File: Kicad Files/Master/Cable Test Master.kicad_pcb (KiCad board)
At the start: 2 copper layers, 50.8 x 61.6 mm, 64 parts, among them J1 RJ45, J2 RJ12, J3 PWR, J4 ISP, Q1 BSS84, Q10 2N7002, Q11 2N7002, Q12 2N7002, Q13 2N7002, Q14 2N7002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

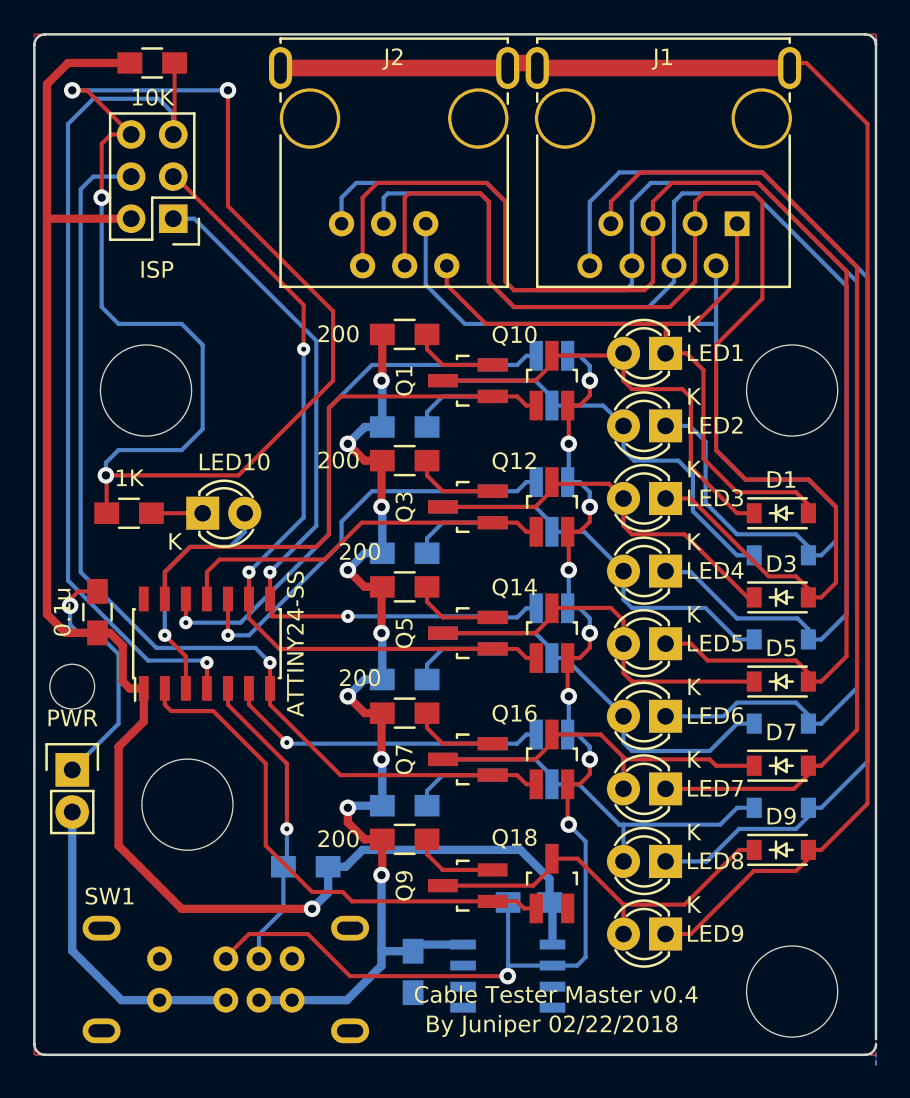
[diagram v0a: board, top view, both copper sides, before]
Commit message: Fix small measurement error in RJ-45 Footprint
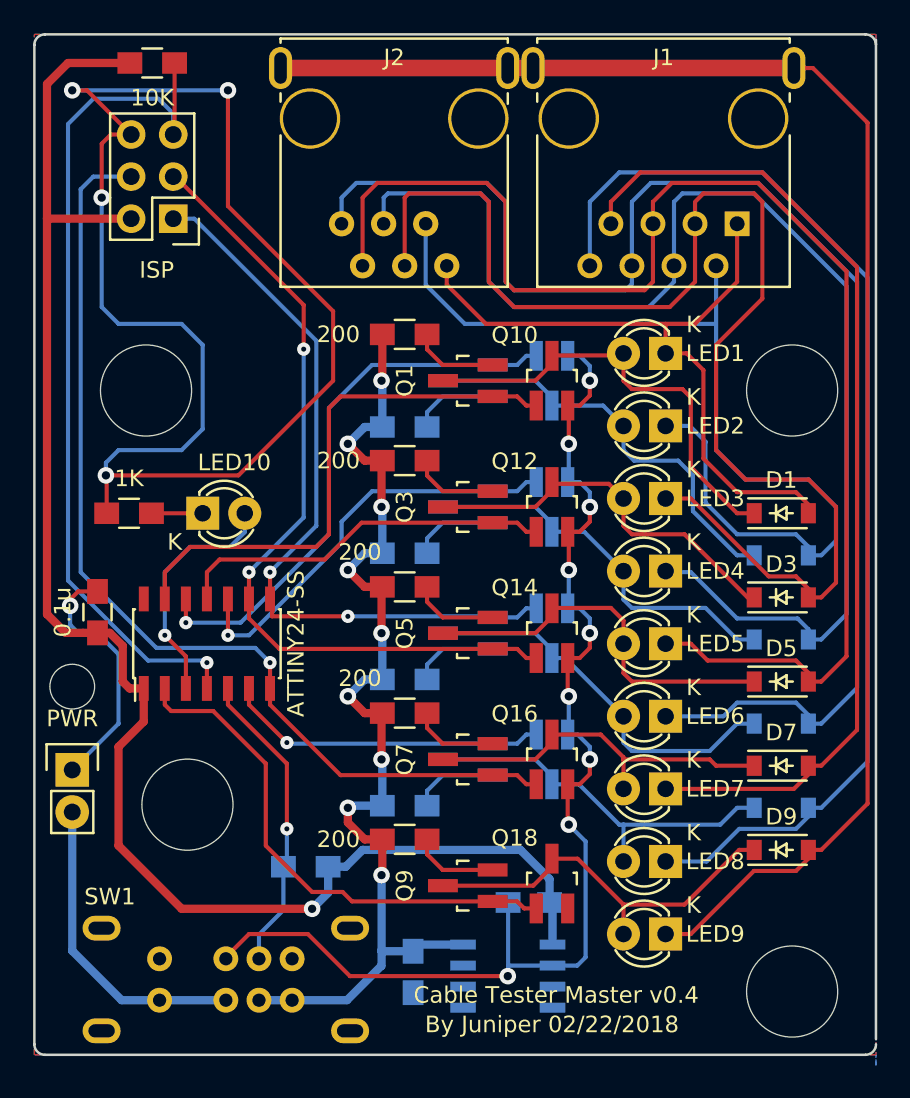
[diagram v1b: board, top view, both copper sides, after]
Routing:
- net /S: track 93.7 -> 93.2 mm
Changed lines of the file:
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@@
     (pad 1 thru_hole circle (at 0 0) (size 5.5 5.5) (drill 5.5) (layers))
-  )
-  (module Tester_Connectors:RJ45_SHLD (layer F.Cu)
-    (at 149.733 68.58 180)
-    (tags RJ45)
-    (fp_text reference J1 (at 0 3.683 180) (layer F.SilkS)
-      (effects (font (size 1 1) (thickness 0.15)))
-    )
-    (fp_text value RJ45 (at 0.14224 -0.1016 180) (layer F.Fab)
-      (effects (font (size 1 1) (thickness 0.15)))
-    )
-    (fp_line (start 7.62 -1.016) (end 7.62 -10.16) (layer F.SilkS) (width 0.15))
-    (fp_line (start 7.62 -10.16) (end -7.62 -10.16) (layer F.SilkS) (width 0.15))
-    (fp_line (start -7.62 -10.16) (end -7.62 -1.016) (layer F.SilkS) (width 0.15))
-    (fp_line (start 7.62 4.572) (end 7.62 4.826) (layer F.SilkS) (width 0.15))
-    (fp_line (start 7.62 4.826) (end -7.62 4.826) (layer F.SilkS) (width 0.15))
-    (fp_line (start -7.62 4.826) (end -7.62 4.572) (layer F.SilkS) (width 0.15))
-    (fp_line (start -7.62 1.524) (end -7.62 1.016) (layer F.SilkS) (width 0.15))
-    (fp_line (start 7.62 1.016) (end 7.62 1.524) (layer F.SilkS) (width 0.15))
-    (pad 9 thru_hole oval (at -7.62 3.048 180) (size 1.397 2.54) (drill oval 0.762 1.905) (layers *.Cu *.Mask F.SilkS)
-      (net 12 /S))
-    (pad "" np_thru_hole circle (at 5.93852 0 180) (size 3.64998 3.64998) (drill 3.2512) (layers *.Cu *.SilkS *.Mask))
-    (pad Hole np_thru_hole circle (at -5.9309 0 180) (size 3.64998 3.64998) (drill 3.2512) (layers *.Cu *.SilkS *.Mask))
-    (pad 1 thru_hole rect (at -4.445 -6.35 180) (size 1.50114 1.50114) (drill 0.89916) (layers *.Cu *.Mask F.SilkS)
-      (net 4 /1))
-    (pad 2 thru_hole circle (at -3.175 -8.89 180) (size 1.50114 1.50114) (drill 0.89916) (layers *.Cu *.Mask F.SilkS)
-      (net 5 /2))
-    (pad 3 thru_hole circle (at -1.905 -6.35 180) (size 1.50114 1.50114) (drill 0.89916) (layers *.Cu *.Mask F.SilkS)
-      (net 6 /3))
-    (pad 4 thru_hole circle (at -0.635 -8.89 180) (size 1.50114 1.50114) (drill 0.89916) (layers *.Cu *.Mask F.SilkS)
-      (net 7 /4))
-    (pad 5 thru_hole circle (at 0.635 -6.35 180) (size 1.50114 1.50114) (drill 0.89916) (layers *.Cu *.Mask F.SilkS)
-      (net 8 /5))
-    (pad 6 thru_hole circle (at 1.905 -8.89 180) (size 1.50114 1.50114) (drill 0.89916) (layers *.Cu *.Mask F.SilkS)
-      (net 9 /6))
-    (pad 7 thru_hole circle (at 3.175 -6.35 180) (size 1.50114 1.50114) (drill 0.89916) (layers *.Cu *.Mask F.SilkS)
-      (net 10 /7))
-    (pad 8 thru_hole circle (at 4.445 -8.89 180) (size 1.50114 1.50114) (drill 0.89916) (layers *.Cu *.Mask F.SilkS)
-      (net 11 /8))
-    (pad 9 thru_hole oval (at 7.62 3.048 180) (size 1.397 2.54) (drill oval 0.762 1.905) (layers *.Cu *.Mask F.SilkS)
-      (net 12 /S))
-    (model Connect.3dshapes/RJ45_8.wrl
-      (at (xyz 0 0 0))
-      (scale (xyz 0.4 0.4 0.4))
-      (rotate (xyz 0 0 0))
-    )
   )
   (module Mounting_Holes:MountingHole_2-7mm locked (layer F.Cu)
@@
     (pad "" np_thru_hole circle (at 5.08 0 180) (size 3.64998 3.64998) (drill 3.2512) (layers *.Cu *.Mask F.SilkS))
     (pad "" np_thru_hole circle (at -5.08 0 180) (size 3.64998 3.64998) (drill 3.2512) (layers *.Cu *.Mask F.SilkS))
+  )
+  (module Tester_Connectors:RJ45_SHLD (layer F.Cu)
+    (at 149.733 68.58 180)
+    (tags RJ45)
+    (fp_text reference J1 (at 0 3.683 180) (layer F.SilkS)
+      (effects (font (size 1 1) (thickness 0.15)))
+    )
+    (fp_text value RJ45 (at 0.14224 -0.1016 180) (layer F.Fab)
+      (effects (font (size 1 1) (thickness 0.15)))
+    )
+    (fp_line (start 7.62 -1.016) (end 7.62 -10.16) (layer F.SilkS) (width 0.15))
+    (fp_line (start 7.62 -10.16) (end -7.62 -10.16) (layer F.SilkS) (width 0.15))
+    (fp_line (start -7.62 -10.16) (end -7.62 -1.016) (layer F.SilkS) (width 0.15))
+    (fp_line (start 7.62 4.572) (end 7.62 4.826) (layer F.SilkS) (width 0.15))
+    (fp_line (start 7.62 4.826) (end -7.62 4.826) (layer F.SilkS) (width 0.15))
+    (fp_line (start -7.62 4.826) (end -7.62 4.572) (layer F.SilkS) (width 0.15))
+    (fp_line (start -7.62 1.524) (end -7.62 1.016) (layer F.SilkS) (width 0.15))
+    (fp_line (start 7.62 1.016) (end 7.62 1.524) (layer F.SilkS) (width 0.15))
+    (pad 9 thru_hole oval (at -7.874 3.048 180) (size 1.397 2.54) (drill oval 0.762 1.905) (layers *.Cu *.Mask F.SilkS)
+      (net 12 /S))
+    (pad "" np_thru_hole circle (at 5.715 0 180) (size 3.64998 3.64998) (drill 3.2512) (layers *.Cu *.SilkS *.Mask))
+    (pad "" np_thru_hole circle (at -5.715 0 180) (size 3.64998 3.64998) (drill 3.2512) (layers *.Cu *.SilkS *.Mask))
+    (pad 1 thru_hole rect (at -4.445 -6.35 180) (size 1.50114 1.50114) (drill 0.89916) (layers *.Cu *.Mask F.SilkS)
+      (net 4 /1))
+    (pad 2 thru_hole circle (at -3.175 -8.89 180) (size 1.50114 1.50114) (drill 0.89916) (layers *.Cu *.Mask F.SilkS)
+      (net 5 /2))
+    (pad 3 thru_hole circle (at -1.905 -6.35 180) (size 1.50114 1.50114) (drill 0.89916) (layers *.Cu *.Mask F.SilkS)
+      (net 6 /3))
+    (pad 4 thru_hole circle (at -0.635 -8.89 180) (size 1.50114 1.50114) (drill 0.89916) (layers *.Cu *.Mask F.SilkS)
+      (net 7 /4))
+    (pad 5 thru_hole circle (at 0.635 -6.35 180) (size 1.50114 1.50114) (drill 0.89916) (layers *.Cu *.Mask F.SilkS)
+      (net 8 /5))
+    (pad 6 thru_hole circle (at 1.905 -8.89 180) (size 1.50114 1.50114) (drill 0.89916) (layers *.Cu *.Mask F.SilkS)
+      (net 9 /6))
+    (pad 7 thru_hole circle (at 3.175 -6.35 180) (size 1.50114 1.50114) (drill 0.89916) (layers *.Cu *.Mask F.SilkS)
+      (net 10 /7))
+    (pad 8 thru_hole circle (at 4.445 -8.89 180) (size 1.50114 1.50114) (drill 0.89916) (layers *.Cu *.Mask F.SilkS)
+      (net 11 /8))
+    (pad 9 thru_hole oval (at 7.874 3.048 180) (size 1.397 2.54) (drill oval 0.762 1.905) (layers *.Cu *.Mask F.SilkS)
+      (net 12 /S))
+    (model Connect.3dshapes/RJ45_8.wrl
+      (at (xyz 0 0 0))
+      (scale (xyz 0.4 0.4 0.4))
+      (rotate (xyz 0 0 0))
+    )
   )
   (gr_line (start 111.76 124.46) (end 111.76 64.135) (layer Edge.Cuts) (width 0.15))
@@
   (segment (start 162.052 107.3912) (end 162.052 78.1812) (width 0.25) (layer B.Cu) (net 11))
   (segment (start 159.258 110.1852) (end 162.052 107.3912) (width 0.25) (layer B.Cu) (net 11))
-  (segment (start 157.353 65.2272) (end 158.369 65.2272) (width 0.25) (layer F.Cu) (net 12) (status 10))
-  (segment (start 159.258 112.7252) (end 158.48 112.7252) (width 0.25) (layer F.Cu) (net 12) (status 20))
-  (segment (start 162.052 109.9312) (end 159.258 112.7252) (width 0.25) (layer F.Cu) (net 12))
-  (segment (start 162.052 68.9102) (end 162.052 109.9312) (width 0.25) (layer F.Cu) (net 12))
-  (segment (start 158.369 65.2272) (end 162.052 68.9102) (width 0.25) (layer F.Cu) (net 12))
+  (segment (start 158.48 112.7252) (end 159.258 112.7252) (width 0.25) (layer F.Cu) (net 12))
+  (segment (start 159.258 112.7252) (end 162.052 109.9312) (width 0.25) (layer F.Cu) (net 12))
+  (segment (start 162.052 109.9312) (end 162.052 68.834) (width 0.25) (layer F.Cu) (net 12))
+  (segment (start 162.052 68.834) (end 158.75 65.532) (width 0.25) (layer F.Cu) (net 12))
+  (segment (start 158.75 65.532) (end 157.607 65.532) (width 0.25) (layer F.Cu) (net 12))
   (segment (start 142.113 65.532) (end 157.353 65.532) (width 1) (layer F.Cu) (net 12) (status 30))
+  (segment (start 140.335 65.532) (end 141.859 65.532) (width 1) (layer F.Cu) (net 12))
   (segment (start 158.48 112.7252) (end 158.48 113.2492) (width 0.25) (layer F.Cu) (net 12) (status 30))
   (segment (start 158.48 113.2492) (end 157.734 113.9952) (width 0.25) (layer F.Cu) (net 12) (status 10))
@@
   (segment (start 155.194 113.9952) (end 151.384 117.8052) (width 0.25) (layer F.Cu) (net 12))
   (segment (start 157.734 113.9952) (end 155.194 113.9952) (width 0.25) (layer F.Cu) (net 12))
-  (segment (start 142.113 65.2272) (end 140.335 65.2272) (width 1) (layer F.Cu) (net 12) (status 30))
   (segment (start 140.335 65.532) (end 126.619 65.532) (width 1) (layer F.Cu) (net 12) (status 30))
   (segment (start 123.317 121.7984) (end 119.317 121.7984) (width 0.5) (layer B.Cu) (net 13) (status 30))
